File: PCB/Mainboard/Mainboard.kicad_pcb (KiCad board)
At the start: 2 copper layers, 1 part, among them J1 Conn_GPS

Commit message: First rev is done
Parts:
- added BT1: BK-18650-PC8, Felix:BAT_BK-18650-PC8, B.Cu at (112.8, 67.0)
- added H1: MountingHole_Pad, MountingHole:MountingHole_3.2mm_M3_Pad, F.Cu at (70.0, 32.0)
- added H2: MountingHole_Pad, MountingHole:MountingHole_3.2mm_M3_Pad, F.Cu at (156.0, 32.0)
- added H3: MountingHole_Pad, MountingHole:MountingHole_3.2mm_M3_Pad, F.Cu at (143.0, 122.0)
- added H4: MountingHole_Pad, MountingHole:MountingHole_3.2mm_M3_Pad, F.Cu at (82.0, 122.0)
- added J2: AS7265X, Connector_PinHeader_2.54mm:PinHeader_1x06_P2.54mm_Vertical, F.Cu at (68.0, 83.5)
- added J3: UV, Connector_PinHeader_2.54mm:PinHeader_1x03_P2.54mm_Vertical, F.Cu at (85.0, 84.0)
- added J4: ADS1115, Connector_PinHeader_2.54mm:PinHeader_1x10_P2.54mm_Vertical, F.Cu at (101.5, 83.0)
- added J5: GPS, Connector_PinHeader_2.54mm:PinHeader_1x04_P2.54mm_Vertical, F.Cu at (68.0, 122.0)
- added J6: GPS, Connector_PinHeader_2.54mm:PinHeader_1x04_P2.54mm_Vertical, F.Cu at (109.5, 122.0)
- added J7: SD-Card, Connector_PinHeader_2.54mm:PinHeader_1x06_P2.54mm_Vertical, F.Cu at (111.0, 101.0)
- added JP1: SolderJumper_3_Open, Jumper:SolderJumper-3_P2.0mm_Open_TrianglePad1.0x1.5mm_NumberLabels, B.Cu at (154.0, 67.0)
- added JP10: SolderJumper_2_Open, Jumper:SolderJumper-2_P1.3mm_Open_TrianglePad1.0x1.5mm, B.Cu at (158.0, 66.7)
- added JP11: SolderJumper_2_Open, Jumper:SolderJumper-2_P1.3mm_Open_TrianglePad1.0x1.5mm, B.Cu at (158.0, 85.3)
- added JP2: SolderJumper_3_Open, Jumper:SolderJumper-3_P2.0mm_Open_TrianglePad1.0x1.5mm_NumberLabels, B.Cu at (154.0, 47.0)
- added JP3: SolderJumper_3_Open, Jumper:SolderJumper-3_P2.0mm_Open_TrianglePad1.0x1.5mm_NumberLabels, B.Cu at (154.0, 85.2)
- added JP4: SolderJumper_2_Open, Jumper:SolderJumper-2_P1.3mm_Open_TrianglePad1.0x1.5mm, B.Cu at (70.0, 38.0)
- added JP5: SolderJumper_2_Open, Jumper:SolderJumper-2_P1.3mm_Open_TrianglePad1.0x1.5mm, B.Cu at (69.7, 57.0)
- added JP6: SolderJumper_2_Open, Jumper:SolderJumper-2_P1.3mm_Open_TrianglePad1.0x1.5mm, B.Cu at (70.0, 77.0)
- added JP9: SolderJumper_2_Open, Jumper:SolderJumper-2_P1.3mm_Open_TrianglePad1.0x1.5mm, B.Cu at (158.0, 46.7)
- added Q1: AO3400A, Package_TO_SOT_SMD:SOT-23, F.Cu at (117.0, 112.9)
- added R1: 47K, Resistor_THT:R_Axial_DIN0411_L9.9mm_D3.6mm_P15.24mm_Horizontal, F.Cu at (134.8, 81.0)
- added R2: 220K, Resistor_THT:R_Axial_DIN0411_L9.9mm_D3.6mm_P15.24mm_Horizontal, F.Cu at (150.0, 86.0)
- added U1: ESP32-DEVKIT-V1, Felix:MODULE_ESP32_DEVKIT_V1_NO_WIFI, F.Cu at (148.5, 52.7)
- added U2: ESP32-DEVKIT-V1, Felix:MODULE_ESP32_DEVKIT_V1_NO_WIFI, F.Cu at (77.5, 52.7)
- added U3: WIFI_KIT_32__V3_, Felix:MODULE_WIFI_KIT_32__V3_, F.Cu at (112.5, 52.3)
- added U4: SIM800L-CORE, Felix_GSM:SIM800L-CORE, F.Cu at (156.0, 93.0)
- J1: value Conn_GPS -> GPS
- moved J1 39.6 mm to (150.4, 122.0), turned to 90 degrees
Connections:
- J1 pad 1: +3.3V -> /GPSModule/VCC
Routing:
- net +3.3V: track 0.00 -> 259.5 mm
- net /GPSModule/VCC: track 0.00 -> 116.8 mm, vias 0 -> 2
- net /RX: track 0.00 -> 105.7 mm
- net /TX: track 0.00 -> 104.2 mm
- net /GPSModule/RX: track 0.00 -> 87.4 mm
- net /GPSModule/TX: track 0.00 -> 86.9 mm
- net /GsmModule/TX: track 0.00 -> 81.7 mm
- net Net-(U2-TX2): track 0.00 -> 81.1 mm, vias 0 -> 1
- net /ADS1115/A0: track 0.00 -> 77.2 mm
- net Net-(U2-RX2): track 0.00 -> 76.4 mm, vias 0 -> 1
- net /SdCard/MISO: track 0.00 -> 64.5 mm
- net /GPSModule1/TX: track 0.00 -> 64.0 mm
- net /ADS1115/A3: track 0.00 -> 61.0 mm
- net /SdCard/MOSI: track 0.00 -> 60.6 mm
- net /GPSModule1/RX: track 0.00 -> 60.3 mm
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- added copper zone on B.Cu, net GND
- added copper zone on F.Cu, net GND
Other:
- board outline added: 100 x 100 mm
- board text added: "+"
- board text added: "-"
- board text added: "Diese Batterie spreist GSM"

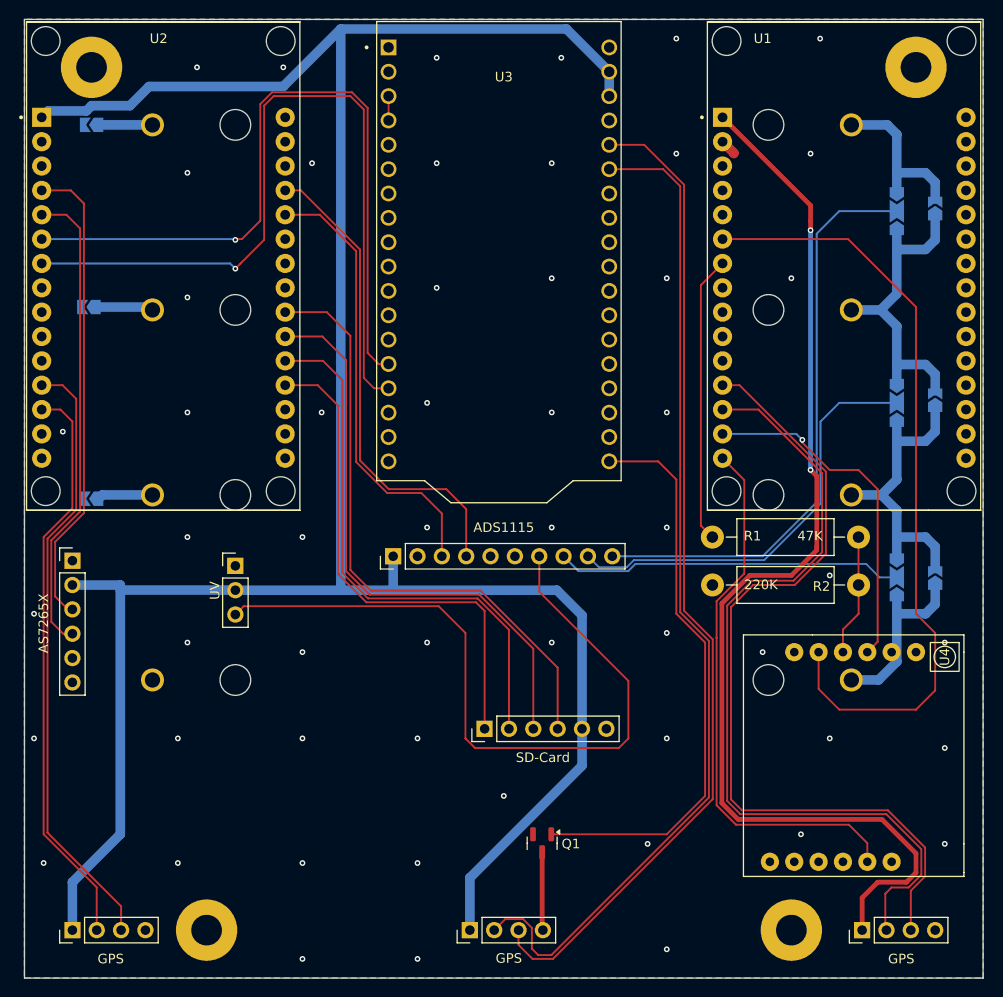
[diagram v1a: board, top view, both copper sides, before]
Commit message: rouned the corners
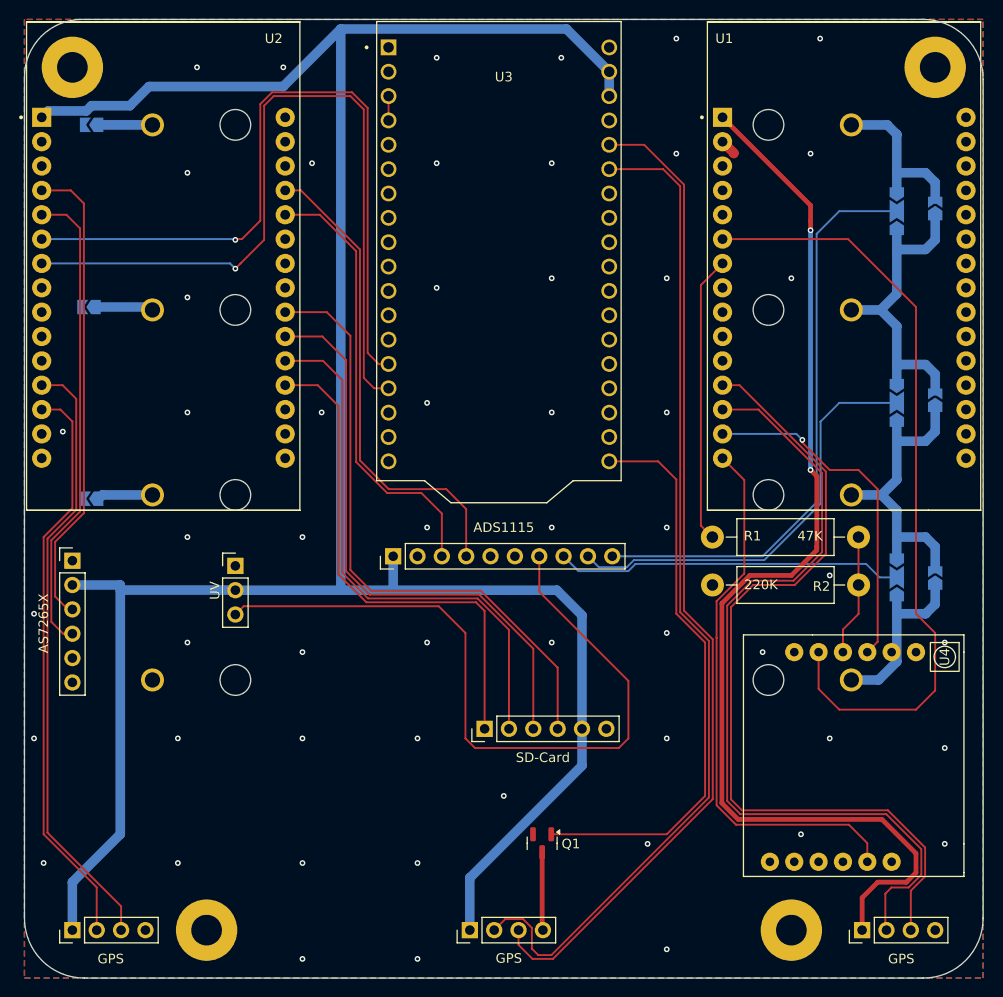
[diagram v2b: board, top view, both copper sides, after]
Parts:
- U1, U2: footprint Felix:MODULE_ESP32_DEVKIT_V1_NO_WIFI -> Felix:MODULE_ESP32_DEVKIT_V1_NO_WIFI_No_Hole
- moved H1 2.00 mm to (68.0, 32.0)
- moved H2 2.00 mm to (158.0, 32.0)
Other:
- outline, holes or cut-outs redrawn
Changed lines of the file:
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@@
 	(footprint "MountingHole:MountingHole_3.2mm_M3_Pad"
 		(layer "F.Cu")
-		(at 156 32)
+		(at 158 32)
 		(descr "Mounting Hole 3.2mm, M3")
 		(tags "mounting hole 3.2mm m3")
@@
 		)
 	)
-	(footprint "Felix:MODULE_ESP32_DEVKIT_V1_NO_WIFI"
+	(footprint "Felix:MODULE_ESP32_DEVKIT_V1_NO_WIFI_No_Hole"
 		(layer "F.Cu")
 		(at 148.518991 52.730908)
 		(property "Reference" "U1"
-			(at -8.518991 -23.730908 0)
+			(at -12.518991 -23.730908 0)
 			(layer "F.SilkS")
 			(effects
@@
 		)
 		(property "Value" "ESP32-DEVKIT-V1"
-			(at -0.518991 -9.730908 0)
+			(at -0.56 27.36 0)
 			(layer "F.Fab")
 			(effects
@@
 			)
 		)
-		(property "Footprint" "Felix:MODULE_ESP32_DEVKIT_V1_NO_WIFI"
+		(property "Footprint" "Felix:MODULE_ESP32_DEVKIT_V1_NO_WIFI_No_Hole"
 			(at 0 0 0)
 			(unlocked yes)
@@
 			(layer "F.Fab")
 		)
-		(pad "" np_thru_hole circle
-			(at -12.28 -23.475)
-			(size 3 3)
-			(drill 3)
-			(layers "*.Cu" "*.Mask")
-		)
-		(pad "" np_thru_hole circle
-			(at -12.28 23.475)
-			(size 3 3)
-			(drill 3)
-			(layers "*.Cu" "*.Mask")
-		)
-		(pad "" np_thru_hole circle
-			(at 12.23 -23.475)
-			(size 3 3)
-			(drill 3)
-			(layers "*.Cu" "*.Mask")
-		)
-		(pad "" np_thru_hole circle
-			(at 12.23 23.475)
-			(size 3 3)
-			(drill 3)
-			(layers "*.Cu" "*.Mask")
-		)
 		(pad "1" thru_hole rect
 			(at -12.7 -15.515)
@@
 		(tags "Through hole pin header THT 1x06 2.54mm single row")
 		(property "Reference" "J2"
-			(at 0 -2.33 360)
+			(at 0 -2.33 0)
 			(layer "F.SilkS")
 			(hide yes)
@@
 	(footprint "MountingHole:MountingHole_3.2mm_M3_Pad"
 		(layer "F.Cu")
-		(at 70 32)
+		(at 68 32)
 		(descr "Mounting Hole 3.2mm, M3")
 		(tags "mounting hole 3.2mm m3")
@@
 		(tags "Through hole pin header THT 1x03 2.54mm single row")
 		(property "Reference" "J3"
-			(at 0 -2.33 360)
+			(at 0 -2.33 0)
 			(layer "F.SilkS")
 			(hide yes)
@@
 		(tags "Through hole pin header THT 1x06 2.54mm single row")
 		(property "Reference" "J7"
-			(at 0 -2.33 270)
+			(at 0 -2.33 -90)
 			(layer "F.SilkS")
 			(hide yes)
@@
 		)
 		(fp_text user "${REFERENCE}"
-			(at 0 6.35 360)
+			(at 0 6.35 0)
 			(layer "F.Fab")
 			(effects
@@
 		(tags "Through hole pin header THT 1x04 2.54mm single row")
 		(property "Reference" "J1"
-			(at 0 -2.33 270)
+			(at 0 -2.33 -90)
 			(layer "F.SilkS")
 			(hide yes)
@@
 		)
 		(fp_text user "${REFERENCE}"
-			(at 0 3.81 360)
+			(at 0 3.81 0)
 			(layer "F.Fab")
 			(effects
@@
 		)
 	)
-	(footprint "Felix:MODULE_ESP32_DEVKIT_V1_NO_WIFI"
+	(footprint "Felix:MODULE_ESP32_DEVKIT_V1_NO_WIFI_No_Hole"
 		(layer "F.Cu")
 		(at 77.49886 52.730908)
 		(property "Reference" "U2"
-			(at -0.49886 -23.730908 0)
+			(at 11.50114 -23.730908 0)
 			(layer "F.SilkS")
 			(effects
@@
 		)
 		(property "Value" "ESP32-DEVKIT-V1"
-			(at 0.50114 -9.730908 0)
+			(at -0.56 27.36 0)
 			(layer "F.Fab")
 			(effects
@@
 			)
 		)
-		(property "Footprint" "Felix:MODULE_ESP32_DEVKIT_V1_NO_WIFI"
+		(property "Footprint" "Felix:MODULE_ESP32_DEVKIT_V1_NO_WIFI_No_Hole"
 			(at 0 0 0)
 			(unlocked yes)
@@
 			(layer "F.Fab")
 		)
-		(pad "" np_thru_hole circle
-			(at -12.28 -23.475)
-			(size 3 3)
-			(drill 3)
-			(layers "*.Cu" "*.Mask")
-		)
-		(pad "" np_thru_hole circle
-			(at -12.28 23.475)
-			(size 3 3)
-			(drill 3)
-			(layers "*.Cu" "*.Mask")
-		)
-		(pad "" np_thru_hole circle
-			(at 12.23 -23.475)
-			(size 3 3)
-			(drill 3)
-			(layers "*.Cu" "*.Mask")
-		)
-		(pad "" np_thru_hole circle
-			(at 12.23 23.475)
-			(size 3 3)
-			(drill 3)
-			(layers "*.Cu" "*.Mask")
-		)
 		(pad "1" thru_hole rect
 			(at -12.7 -15.515)
@@
 		(tags "Through hole pin header THT 1x04 2.54mm single row")
 		(property "Reference" "J6"
-			(at 0 -2.33 270)
+			(at 0 -2.33 -90)
 			(layer "F.SilkS")
 			(hide yes)
@@
 		)
 		(fp_text user "${REFERENCE}"
-			(at 0 3.81 360)
+			(at 0 3.81 0)
 			(layer "F.Fab")
 			(effects
@@
 		(tags "Through hole pin header THT 1x10 2.54mm single row")
 		(property "Reference" "J4"
-			(at 0 -2.33 270)
+			(at 0 -2.33 -90)
 			(layer "F.SilkS")
 			(hide yes)
@@
 		)
 		(fp_text user "${REFERENCE}"
-			(at 0 11.43 360)
+			(at 0 11.43 0)
 			(layer "F.Fab")
 			(effects
@@
 		(tags "Through hole pin header THT 1x04 2.54mm single row")
 		(property "Reference" "J5"
-			(at 0 -2.33 270)
+			(at 0 -2.33 -90)
 			(layer "F.SilkS")
 			(hide yes)
@@
 		)
 		(fp_text user "${REFERENCE}"
-			(at 0 3.81 360)
+			(at 0 3.81 0)
 			(layer "F.Fab")
 			(effects
@@
 		(tags "solder jumper open")
 		(property "Reference" "JP9"
-			(at -3.275 0 270)
+			(at -3.275 0 -90)
 			(layer "B.SilkS")
 			(effects
@@
 		)
 		(property "Value" "SolderJumper_2_Open"
-			(at 0 -1.9 270)
+			(at 0 -1.9 -90)
 			(layer "B.Fab")
 			(hide yes)
@@
 		(tags "solder jumper open")
 		(property "Reference" "JP11"
-			(at -3.725 0 270)
+			(at -3.725 0 -90)
 			(layer "B.SilkS")
 			(effects
@@
 		)
 		(property "Value" "SolderJumper_2_Open"
-			(at 0 -1.9 270)
+			(at 0 -1.9 -90)
 			(layer "B.Fab")
 			(hide yes)
@@
 		(tags "solder jumper open")
 		(property "Reference" "JP10"
-			(at -3.275 0 270)
+			(at -3.275 0 -90)
 			(layer "B.SilkS")
 			(effects
@@
 		)
 		(property "Value" "SolderJumper_2_Open"
-			(at 0 -1.9 270)
+			(at 0 -1.9 -90)
 			(layer "B.Fab")
 			(hide yes)
@@
 		)
 	)
-	(gr_rect
-		(start 63 27)
-		(end 163 127)
+	(gr_line
+		(start 163 120.757359)
+		(end 163 33.242641)
+		(stroke
+			(width 0.05)
+			(type default)
+		)
+		(layer "Edge.Cuts")
+	)
+	(gr_line
+		(start 63 33)
+		(end 63 120.757359)
+		(stroke
+			(width 0.05)
+			(type default)
+		)
+		(layer "Edge.Cuts")
+	)
+	(gr_arc
+		(start 69.242641 127)
+		(mid 64.828427 125.171573)
+		(end 63 120.757359)
+		(stroke
+			(width 0.05)
+			(type default)
+		)
+		(layer "Edge.Cuts")
+	)
+	(gr_arc
+		(start 156.757359 27)
+		(mid 161.171573 28.828427)
+		(end 163 33.242641)
+		(stroke
+			(width 0.05)
+			(type default)
+		)
+		(layer "Edge.Cuts")
+	)
+	(gr_arc
+		(start 63 33)
+		(mid 64.757359 28.757359)
+		(end 69 27)
+		(stroke
+			(width 0.05)
+			(type default)
+		)
+		(layer "Edge.Cuts")
+	)
+	(gr_line
+		(start 69.242641 127)
+		(end 156.757359 127)
+		(stroke
+			(width 0.05)
+			(type default)
+		)
+		(layer "Edge.Cuts")
+	)
+	(gr_arc
+		(start 163 120.757359)
+		(mid 161.171573 125.171573)
+		(end 156.757359 127)
+		(stroke
+			(width 0.05)
+			(type default)
+		)
+		(layer "Edge.Cuts")
+	)
+	(gr_line
+		(start 156.757359 27)
+		(end 69 27)
 		(stroke
 			(width 0.05)
 			(type default)
 		)
-		(fill none)
 		(layer "Edge.Cuts")
 	)
